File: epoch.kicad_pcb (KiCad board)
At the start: 2 copper layers, 30 x 30 mm, 26 parts, among them P1 USB_OTG, P3 CONN_01X10, P4 CONN_02X05, SW1 SW_Reset, SW2 SW_Up, SW3 SW_Middle, SW4 SW_Down, U1 MIC5219-3.3BM5, U2 ATSAMD21Ennc-AU, U3 DS3231MZ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

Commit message: More Layout
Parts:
- removed P1: USB_OTG, Connectors_Molex:USB_Micro-B_Molex_47346-0001
- added J1: USB_OTG, Connectors:USB-MICROB_LARGEPAD, F.Cu at (151.2, 113.9)
- moved C6 51.2 mm to (155.2, 103.0), turned to 90 degrees
- moved C3 47.5 mm to (151.9, 121.8), turned to 270 degrees
- moved R3 42.5 mm to (173.8, 111.9), turned to 90 degrees
- moved R1 41.8 mm to (169.2, 128.4)
- moved C5 40.9 mm to (151.2, 106.8)
- moved C11 39.2 mm to (156.0, 108.8), turned to 180 degrees
- moved P4 35.8 mm to (188.5, 104.5)
- moved R2 35.0 mm to (176.3, 111.9), turned to 90 degrees
- moved C9 34.7 mm to (171.5, 112.4), turned to 90 degrees
- moved R5 30.1 mm to (175.0, 115.7)
- moved C1 30.0 mm to (170.0, 121.5), turned to 270 degrees
- moved C2 15.4 mm to (149.4, 121.8), turned to 270 degrees
- moved C7 12.3 mm to (163.3, 123.8), turned to 180 degrees
- moved C4 12.1 mm to (169.2, 125.9)
- moved U1 8.59 mm to (151.4, 103.5)
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
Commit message: Start connecting
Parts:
- J1: moved to B.Cu
- moved U5 12.1 mm to (168.2, 108.3), turned to 180 degrees
- moved C2 7.06 mm to (155.5, 118.2), turned to 180 degrees
- moved C3 6.84 mm to (155.5, 115.9), turned to 180 degrees
- moved C7 6.40 mm to (157.0, 124.6), turned to 90 degrees
- moved Y1 4.75 mm to (161.8, 124.8), turned to 270 degrees
- moved C8 2.90 mm to (165.1, 124.8), turned to 90 degrees
- moved J1 2.81 mm to (150.9, 116.7), turned to 90 degrees
- moved R2 2.54 mm to (173.8, 111.9)
- moved R3 2.54 mm to (176.3, 111.9)
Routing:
- net Net-(J1-Pad1): track 0.00 -> 26.3 mm, vias 0 -> 1
- net (GND): track 0.00 -> 23.9 mm, vias 0 -> 1
- net SPI_SI: track 0.00 -> 7.56 mm
- net VCOM: track 0.00 -> 6.15 mm
- net Net-(C7-Pad2): track 0.00 -> 6.10 mm
- net Net-(C8-Pad2): track 0.00 -> 5.89 mm
- net SPI_CS: track 0.00 -> 5.24 mm
- net SPI_CLK: track 0.00 -> 4.99 mm
- net (+3.3): track 0.00 -> 3.72 mm
- net SCL: track 0.00 -> 3.54 mm
- net SDA: track 0.00 -> 3.11 mm
- net Net-(C3-Pad1): track 0.00 -> 2.67 mm
- net Net-(C5-Pad2): track 0.00 -> 2.40 mm
- added copper zone on F.Cu, net (GND)
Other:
- net class Default: clearance 0.2 -> 0.1524; trace_width 0.25 -> 0.1524; via_dia 0.6 -> 0.6858; via_drill 0.4 -> 0.3302
- rule trace_clearance: 0.2 -> 0.1524
- rule trace_min: 0.2 -> 0.1524
- rule via_min_drill: 0.3 -> 0.3302
- rule via_min_size: 0.4 -> 0.6858

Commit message: Add coincell
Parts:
- added BT1: Battery_Cell, my-fp-library:CR2032-001, B.Cu at (204.0, 104.8)
- C7, C8: value ??uF -> 4.7pF
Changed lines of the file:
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@@
 (kicad_pcb (version 4) (host pcbnew 4.0.5)
   (general
-    (links 79)
-    (no_connects 46)
+    (links 81)
+    (no_connects 48)
     (area 147.924999 99.924999 178.075001 130.075001)
     (thickness 1.6)
@@
     (tracks 78)
     (zones 0)
-    (modules 26)
-    (nets 44)
+    (modules 27)
+    (nets 45)
   )
   (page A4)
@@
     (mod_text_size 1 1)
     (mod_text_width 0.15)
-    (pad_size 1.524 1.524)
-    (pad_drill 0.762)
+    (pad_size 17.8 17.8)
+    (pad_drill 0)
     (pad_to_mask_clearance 0.2)
     (aux_axis_origin 0 0)
@@
   (net 42 "Net-(J1-Pad1)")
   (net 43 "Net-(J1-Pad4)")
+  (net 44 BAT_3.3V)
   (net_class Default "This is the default net class."
     (clearance 0.1524)
@@
     (add_net "(+3.3)")
     (add_net "(GND)")
+    (add_net BAT_3.3V)
     (add_net BUT_DWN)
     (add_net BUT_MID)
@@
       (effects (font (size 1 1) (thickness 0.15)))
     )
-    (fp_text value ??uF (at 0 1.75 90) (layer F.Fab)
+    (fp_text value 4.7pF (at 0 1.75 90) (layer F.Fab)
       (effects (font (size 1 1) (thickness 0.15)))
     )
@@
       (effects (font (size 1 1) (thickness 0.15)))
     )
-    (fp_text value ??uF (at 0 1.75 90) (layer F.Fab)
+    (fp_text value 4.7pF (at 0 1.75 90) (layer F.Fab)
       (effects (font (size 1 1) (thickness 0.15)))
     )
@@
       (net 43 "Net-(J1-Pad4)"))
   )
+  (module my-fp-library:CR2032-001 (layer B.Cu)
+    (at 203.99 104.772 315)
+    (fp_text reference BT1 (at 0 -11.999999 315) (layer B.SilkS)
+      (effects (font (size 1 1) (thickness 0.15)) (justify mirror))
+    )
+    (fp_text value Battery_Cell (at 0.1 12.1 315) (layer B.Fab)
+      (effects (font (size 1 1) (thickness 0.15)) (justify mirror))
+    )
+    (fp_line (start 10 -4.5) (end 7.5 -7) (layer B.Fab) (width 0.1))
+    (fp_line (start 7.5 -7) (end 0 -6) (layer B.Fab) (width 0.1))
+    (fp_line (start 0 -6) (end -7.5 -7) (layer B.Fab) (width 0.1))
+    (fp_line (start -7.5 -7) (end -10 -4.5) (layer B.Fab) (width 0.1))
+    (fp_line (start -10 3.5) (end -8.5 5.5) (layer B.Fab) (width 0.1))
+    (fp_line (start -8.5 5.5) (end 8.5 5.5) (layer B.Fab) (width 0.1))
+    (fp_line (start 8.5 5.5) (end 10 3.5) (layer B.Fab) (width 0.1))
+    (fp_line (start 10 3.5) (end 10 -4.5) (layer B.Fab) (width 0.1))
+    (fp_line (start -10 3.5) (end -10 -4.5) (layer B.Fab) (width 0.1))
+    (fp_circle (center 0 0) (end 7.2 6.2) (layer B.SilkS) (width 0.1))
+    (fp_text user -ve (at 0 -3.5 315) (layer B.SilkS)
+      (effects (font (size 2 2) (thickness 0.15)) (justify mirror))
+    )
+    (fp_text user + (at -11.5 1.5 315) (layer B.SilkS)
+      (effects (font (size 1.5 1.5) (thickness 0.15)) (justify mirror))
+    )
+    (fp_text user + (at 11.4 1.3 315) (layer B.SilkS)
+      (effects (font (size 1.5 1.5) (thickness 0.15)) (justify mirror))
+    )
+    (pad 1 smd rect (at -11.45 0 315) (size 2.5 5.1) (layers B.Cu B.Paste B.Mask)
+      (net 44 BAT_3.3V))
+    (pad 1 smd rect (at 11.45 0 315) (size 2.5 5.1) (layers B.Cu B.Paste B.Mask)
+      (net 44 BAT_3.3V))
+    (pad 2 smd circle (at 0 0 315) (size 17.8 17.8) (layers B.Cu B.Paste B.Mask)
+      (net 2 "(GND)"))
+  )
   (gr_line (start 148 130) (end 148 100) (angle 90) (layer Edge.Cuts) (width 0.15))
   (gr_line (start 178 130) (end 148 130) (angle 90) (layer Edge.Cuts) (width 0.15))
@@
   (segment (start 157 117.218) (end 157.508 117.218) (width 0.25) (layer F.Cu) (net 1))
   (segment (start 156.726 117.492) (end 157 117.218) (width 0.25) (layer F.Cu) (net 1))
-  (segment (start 167.854 117.44) (end 169.414 117.44) (width 0.1524) (layer F.Cu) (net 2) (status 400000))
+  (segment (start 167.854 117.44) (end 169.414 117.44) (width 0.1524) (layer F.Cu) (net 2))
   (segment (start 169.414 117.44) (end 171.478 115.376) (width 0.1524) (layer F.Cu) (net 2))
-  (segment (start 171.478 115.376) (end 171.478 113.642) (width 0.1524) (layer F.Cu) (net 2) (status 800000))
+  (segment (start 171.478 115.376) (end 171.478 113.642) (width 0.1524) (layer F.Cu) (net 2))
   (segment (start 149.908 105.554) (end 149.908 106.804) (width 0.1524) (layer F.Cu) (net 2))
   (segment (start 149.888 105.534) (end 149.908 105.554) (width 0.1524) (layer F.Cu) (net 2))

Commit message: Battery parts
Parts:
- added C10: 1uF, Capacitors_SMD:C_0805_HandSoldering, B.Cu at (165.8, 104.3)
- added D1: ZLLS410, Diodes_SMD:D_SOD-323_HandSoldering, B.Cu at (165.6, 102.1)
- added Q1: DMP1045U, TO_SOT_Packages_SMD:SOT-23_Handsoldering, B.Cu at (160.6, 103.2)
- moved U1 16.3 mm to (150.7, 119.8)
- moved C5 14.4 mm to (155.5, 120.5), turned to 180 degrees
- moved C6 12.5 mm to (151.7, 114.9)
- moved R5 11.3 mm to (174.0, 104.4)
- moved R3 5.85 mm to (176.1, 117.7)
- moved R2 5.84 mm to (173.8, 117.7)
- moved C9 5.21 mm to (171.5, 117.6)
- moved U3 5.18 mm to (174.3, 109.9)
- moved BT1 4.83 mm to (203.7, 109.6), turned to 225 degrees
- moved C1 2.01 mm to (169.3, 123.4), turned to 0 degrees
- moved C11 0.90 mm to (156.9, 108.7)
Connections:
- BT1 pad 1: BAT_3.3V -> Net-(BT1-Pad1)
- C6 pad 1: (+3.3) -> Net-(C6-Pad1)
- U1 pad 5: (+3.3) -> Net-(C6-Pad1)
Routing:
- net Net-(J1-Pad1): track 26.3 -> 0.64 mm, vias 1 -> 0
- net (GND): track 23.9 -> 12.6 mm
- net SCL: track 3.54 -> 0.00 mm
- net SDA: track 3.11 -> 0.00 mm
- net Net-(C5-Pad2): track 2.40 -> 0.00 mm

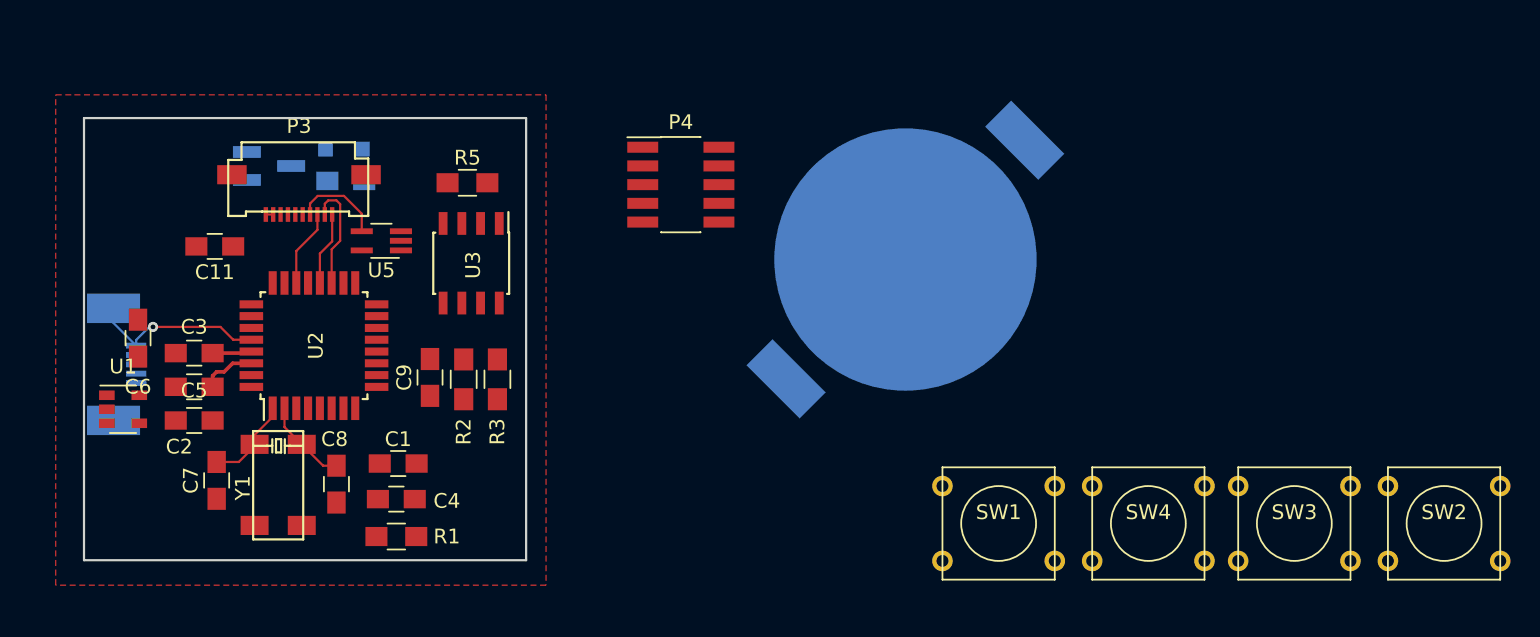
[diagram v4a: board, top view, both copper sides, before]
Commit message: More connections and change battery to pads
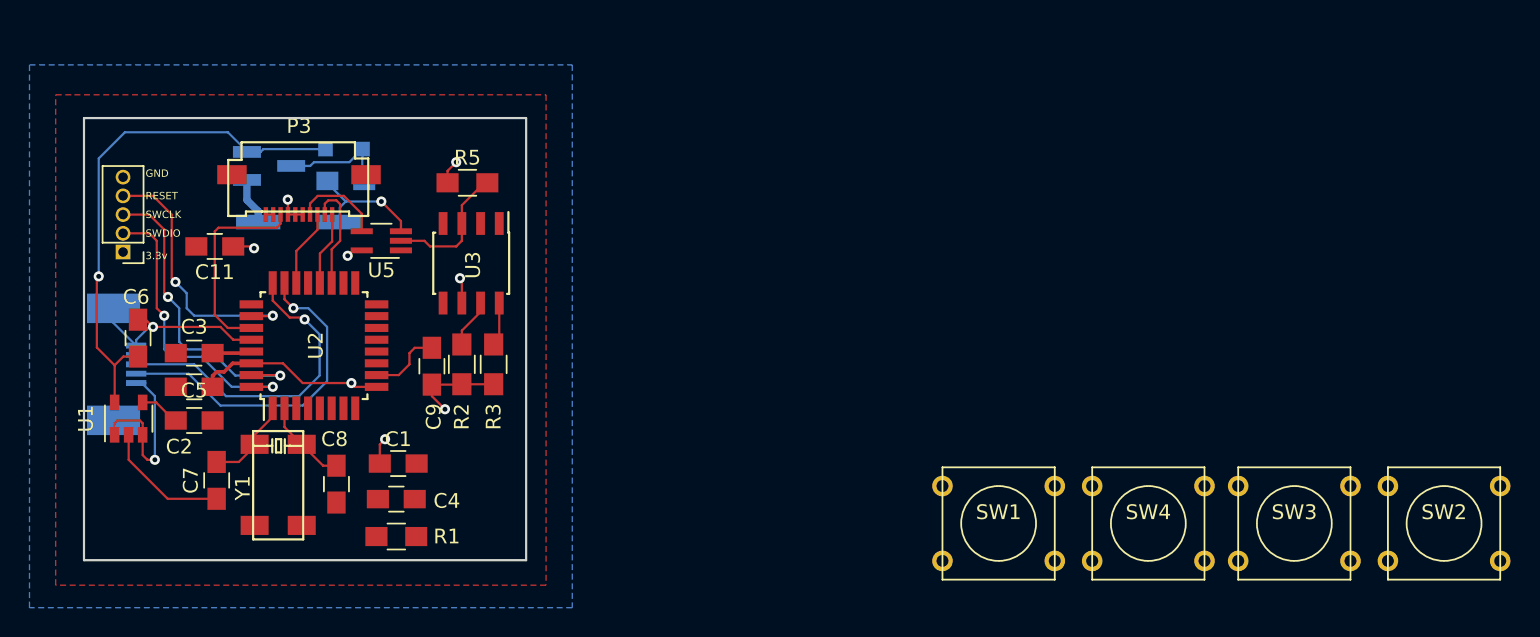
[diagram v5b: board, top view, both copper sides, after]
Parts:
- removed P4: CONN_02X05, Pin_Headers:Pin_Header_Straight_2x05_Pitch1.27mm_SMD
- added J2: CONN_01X05, Pin_Headers:Pin_Header_Straight_1x05_Pitch1.27mm, F.Cu at (150.7, 109.1)
- BT1: footprint my-fp-library:CR2032-001 -> Pin_Headers:Pin_Header_Straight_2x01_Pitch2.54mm_SMD
- P3: footprint Connector_FFC_FPC:MOLEX_0.5MM_505278 -> my-fp-library:MOLEX_0.5MM_505278
- moved BT1 41.2 mm to (162.6, 107.1), turned to 0 degrees
- moved R3 1.05 mm to (175.8, 116.7)
- moved R2 1.02 mm to (173.6, 116.7)
- moved C9 0.77 mm to (171.6, 116.8), turned to 270 degrees
- moved U1 0.74 mm to (151.0, 120.4), turned to 90 degrees
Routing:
- net Net-(C6-Pad1): track 0.00 -> 35.7 mm, vias 0 -> 1
- net (+3.3): track 3.72 -> 37.2 mm, vias 0 -> 8
- net (GND): track 12.6 -> 36.0 mm, vias 1 -> 2
- net USB_D-: track 0.00 -> 23.0 mm, vias 0 -> 1
- net USB_D+: track 0.00 -> 22.0 mm, vias 0 -> 1
- net SWDCLK: track 0.00 -> 21.4 mm, vias 0 -> 2
- net SWDIO: track 0.00 -> 19.9 mm, vias 0 -> 2
- net RESET: track 0.00 -> 18.1 mm, vias 0 -> 2
- net EXTMODE: track 0.00 -> 13.8 mm
- net Net-(J1-Pad1): track 0.64 -> 12.6 mm, vias 0 -> 1
- net Net-(R5-Pad2): track 0.00 -> 9.22 mm
- net Net-(BT1-Pad1): track 0.00 -> 3.66 mm
- net SDA: track 0.00 -> 3.33 mm
- net SCL: track 0.00 -> 2.97 mm
- net Net-(C5-Pad2): track 0.00 -> 2.75 mm
- added copper zone on B.Cu, net (+3.3)
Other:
- board text added: "3.3V"
- board text added: "3.3v"
- board text added: "GND"
- board text added: "RESET"
- board text added: "SWCLK"
- board text added: "SWDIO"

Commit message: Complete connections
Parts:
- SW1: footprint Buttons_Switches_THT:SW_PUSH_SMALL -> Buttons_Switches_SMD:SW_SPST_B3U-1100P
- SW2, SW3, SW4: footprint Buttons_Switches_THT:SW_PUSH_SMALL -> Buttons_Switches_SMD:SW_SPST_B3U-1100P; moved to B.Cu
- moved SW2 64.6 mm to (176.1, 121.0), turned to 270 degrees
- moved SW3 55.7 mm to (176.1, 114.2), turned to 270 degrees
- moved SW4 48.2 mm to (176.1, 108.3), turned to 270 degrees
- moved SW1 34.0 mm to (176.1, 126.6), turned to 90 degrees
- turned R1 to 180 degrees
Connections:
- U2 pad 16: BUT_DWN -> BUT_MID
- U2 pad 21: BUT_MID -> BUT_DWN
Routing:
- net RESET: track 18.1 -> 37.5 mm, vias 2 -> 4
- net SCL: track 2.97 -> 18.3 mm
- net BUT_DWN: track 0.00 -> 14.9 mm, vias 0 -> 1
- net (GND): track 36.0 -> 49.3 mm, vias 2 -> 5
- net BUT_UP: track 0.00 -> 12.5 mm, vias 0 -> 1
- net SDA: track 3.33 -> 13.6 mm
- net BUT_MID: track 0.00 -> 7.51 mm, vias 0 -> 1
- net Net-(R1-Pad1): track 0.00 -> 4.72 mm
- net (+3.3): track 37.2 -> 41.8 mm, vias 8 -> 7

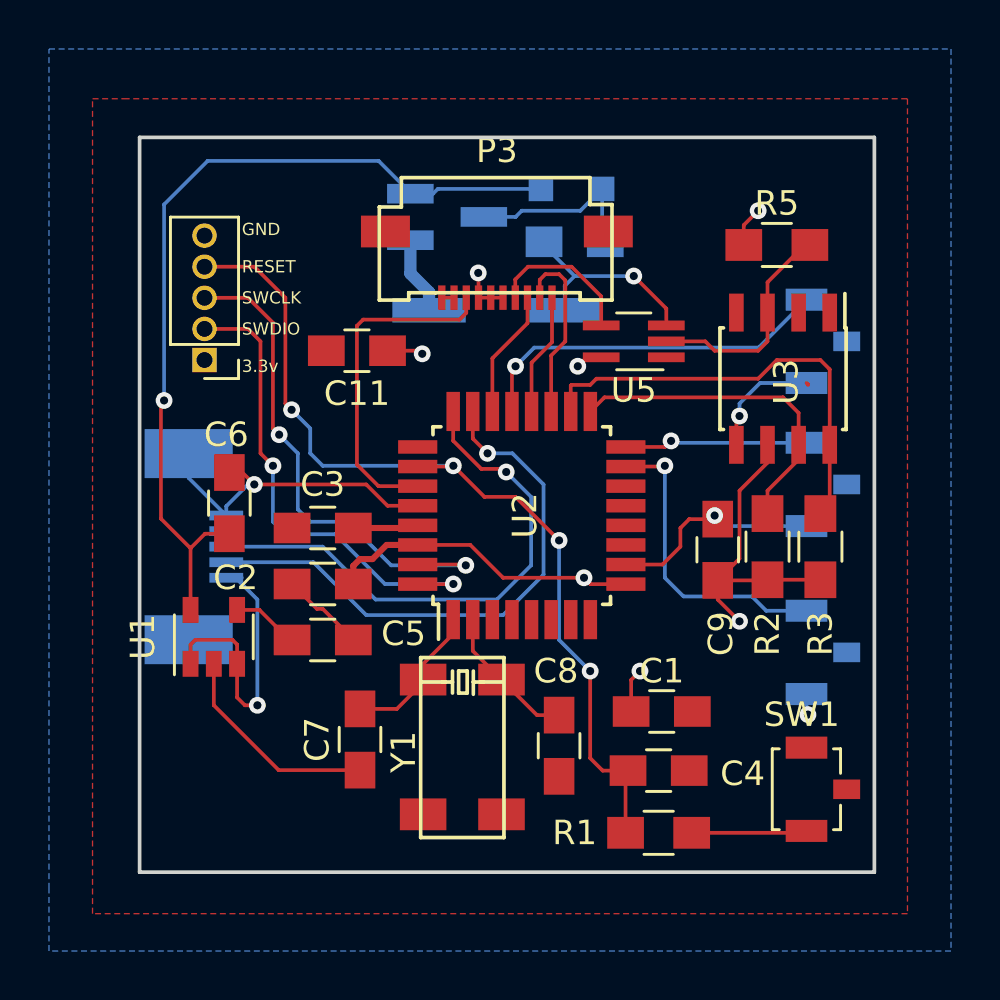
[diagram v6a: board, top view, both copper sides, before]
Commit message: Add LIPO charging
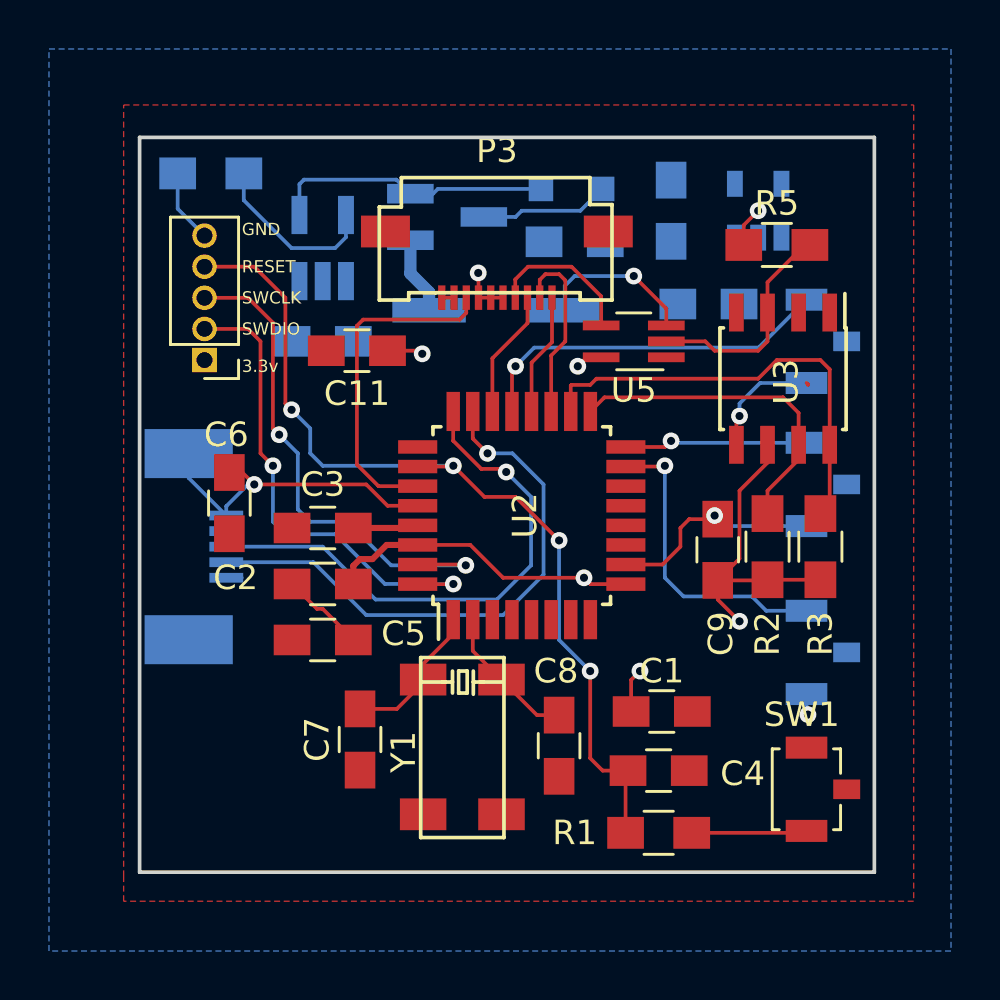
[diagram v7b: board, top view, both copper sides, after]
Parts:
- added C12: 4.7uF, Capacitors_SMD:C_0805_HandSoldering, B.Cu at (155.5, 108.3)
- added C13: 1uF, Capacitors_SMD:C_0805_HandSoldering, B.Cu at (169.7, 103.0)
- added C14: 0.1uF, Capacitors_SMD:C_0805_HandSoldering, B.Cu at (171.2, 106.8)
- added R4: 22K, Resistors_SMD:R_0805_HandSoldering, B.Cu at (150.9, 101.5)
- added U4: MCP73831T-2ACI/OT, TO_SOT_Packages_SMD:SOT-23-5_HandSoldering, B.Cu at (155.5, 104.5)
- C10: value 1uF -> 4.7uF
- C6: value 10uF -> 4.7uF
- U1: moved to B.Cu
- moved U1 28.2 mm to (173.3, 103.0)
- turned C10 to 0 degrees
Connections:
- C10 pad 1: (+3.3) -> Net-(C10-Pad1)
- C6 pad 1: Net-(C6-Pad1) -> (+3.3)
- D1 pad 1: (+3.3) -> (+5)
- D1 pad 2: Net-(C6-Pad1) -> Net-(C10-Pad1)
- J1 pad 1: Net-(J1-Pad1) -> Net-(C10-Pad1)
- Q1 pad 2: Net-(C6-Pad1) -> Net-(C10-Pad1)
- Q1 pad 3: (+3.3) -> (+5)
- U1 pad 1: Net-(J1-Pad1) -> (+5)
- U1 pad 3: Net-(J1-Pad1) -> (+5)
- U1 pad 5: Net-(C6-Pad1) -> (+3.3)
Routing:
- net Net-(C6-Pad1): track 35.7 -> 0.00 mm, vias 1 -> 0
- net Net-(C10-Pad1): track 0.00 -> 12.7 mm
- net Net-(J1-Pad1): track 12.6 -> 0.00 mm, vias 1 -> 0
- net (+3.3): track 41.8 -> 34.3 mm
- net (GND): track 49.3 -> 41.8 mm
- net Net-(R4-Pad1): track 0.00 -> 7.17 mm
- net (+5): track 0.00 -> 5.30 mm
- net Net-(C5-Pad2): track 2.75 -> 0.11 mm
